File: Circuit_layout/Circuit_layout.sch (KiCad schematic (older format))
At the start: 34 parts, among them Q3 MMBF170, SW1 SW_PUSH, SW3 JS202011CQN, U17 MCP6004, U4 LM95071-Q1, U7 AT90CAN128-A, U9 TLP293, Y1 10MHz

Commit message: Completed errata changes
Committing before annotation, footprint assignment, and board relayout for backup purposes
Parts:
- Q3: symbol MMBF170 -> MMBF170-RESCUE-Circuit_layout
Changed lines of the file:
@@
 $EndComp
 $Comp
-L MMBF170 Q3
+L MMBF170-RESCUE-Circuit_layout Q3
 U 1 1 58D1260E
 P 5100 5350

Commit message: Associated footprints and generated new netlist
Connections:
- no-connect marks 20 -> 21
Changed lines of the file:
@@
 Wire Wire Line
 	9800 2000 9850 2000
+NoConn ~ 10450 3400
 $EndSCHEMATC

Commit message: Wider traces for DC/DC converter
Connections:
- no-connect marks 21 -> 20
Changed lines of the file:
@@
 Wire Wire Line
 	9800 2000 9850 2000
-NoConn ~ 10450 3400
 $EndSCHEMATC

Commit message: Generated gerber and drill files for board ordering
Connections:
- net CC_LED_CTRL renamed SPARE_LED_CTRL
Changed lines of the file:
@@
 F5 "Spare_Red" I L 11850 4150 60
 F6 "Spare_Blue" I L 11850 4300 60
-F7 "CC_LED_CTRL" I L 11850 3850 60
+F7 "SPARE_LED_CTRL" I L 11850 3850 60
 $EndSheet
 $Sheet
@@
 	8850 1250 8850 1150
 Text Label 11250 3850 0    60   ~ 0
-CC_LED_CTRL
+SPARE_LED_CTRL
 Wire Wire Line
 	11250 3850 11850 3850
@@
 	11250 4300 11850 4300
 Text Label 9850 2000 0    60   ~ 0
-CC_LED_CTRL
+SPARE_LED_CTRL
 Wire Wire Line
 	9800 2000 9850 2000

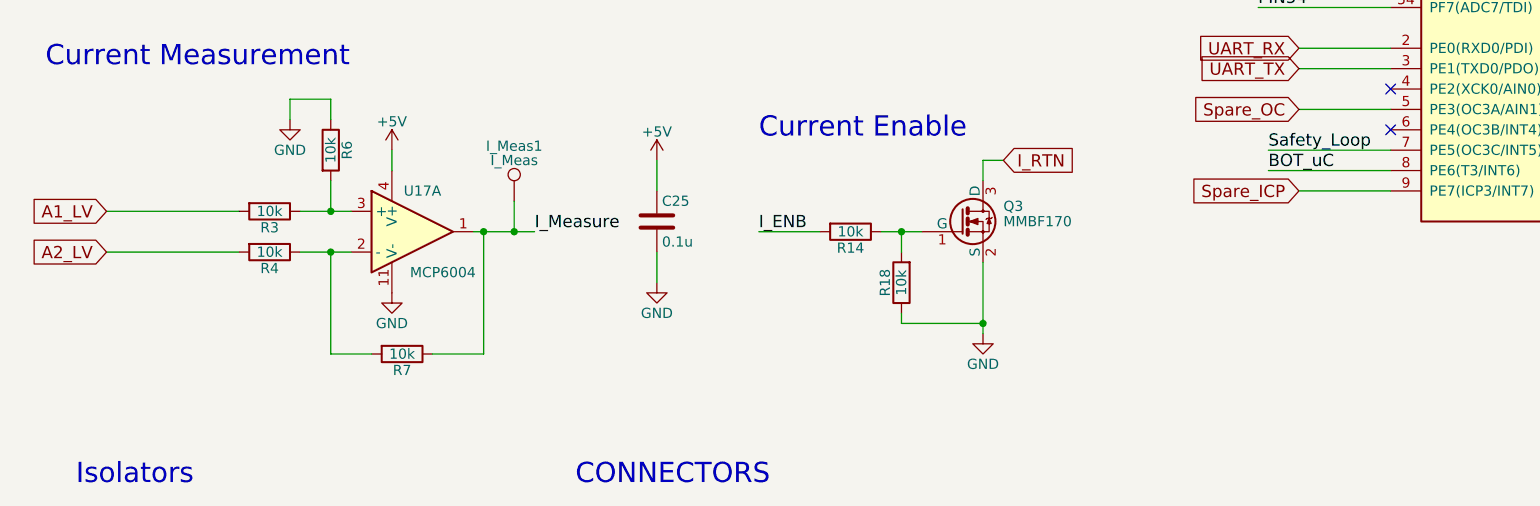
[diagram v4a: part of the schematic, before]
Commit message: Schematic update
Changed schematic to reflect board as assembeled
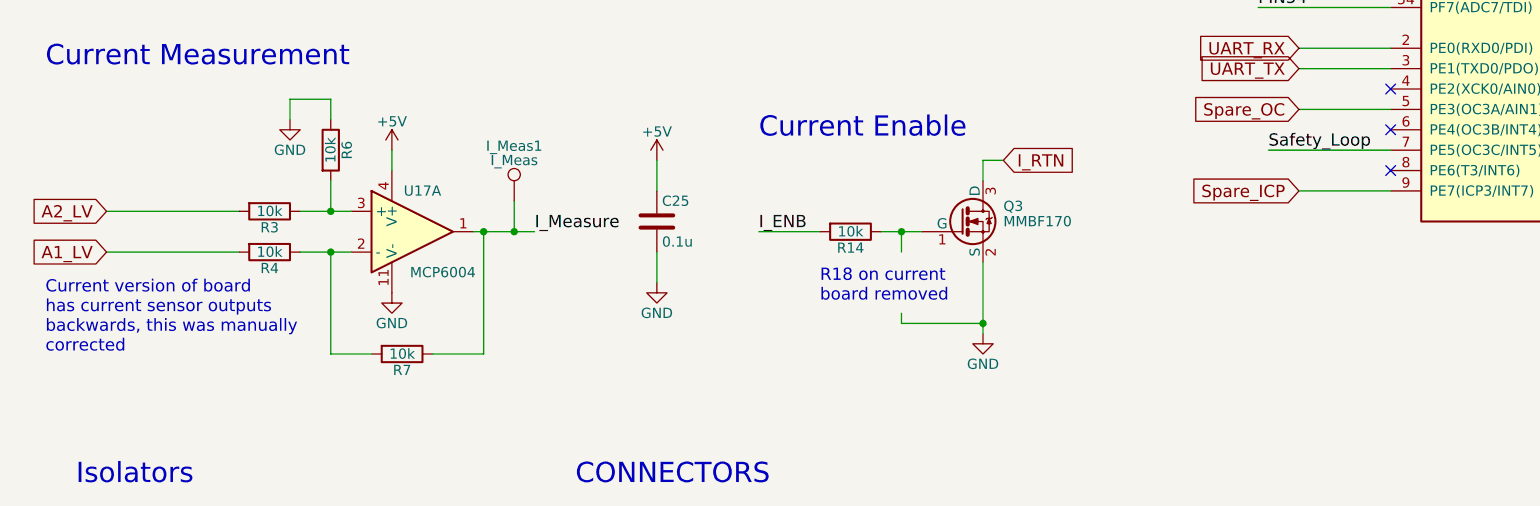
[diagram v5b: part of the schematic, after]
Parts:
- removed R18: 10k, Resistors_SMD:R_0805_HandSoldering, symbol R
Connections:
- net A1_LV: now also R4.2; no longer R3.2
- net A2_LV: now also R3.2; no longer R4.2
- net BOT_uC: no longer U7.8 (PE6(T3/INT6))
- no-connect marks 20 -> 21
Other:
- note added: "Current version of board\nhas current sensor outputs\nbackwards, this was manually\ncorrected"
- note added: "R18 on current\nboard removed"
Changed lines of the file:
@@
 LIBS:ftdi
 LIBS:gennum
-LIBS:graphic
 LIBS:hc11
 LIBS:intel
@@
 LIBS:Lattice
 LIBS:linear
-LIBS:logo
 LIBS:maxim
 LIBS:memory
@@
 Text Label 10450 3400 2    60   ~ 0
 Throttle_uC
+Text GLabel 900  5300 0    60   Input ~ 0
+A2_LV
 Text GLabel 900  5500 0    60   Input ~ 0
-A2_LV
-Text GLabel 900  5300 0    60   Input ~ 0
 A1_LV
 Text GLabel 9900 2300 2    60   Input ~ 0
@@
 Text Label 11100 6250 0    60   ~ 0
 BOT_uC
-Text Label 6600 5100 0    60   ~ 0
-BOT_uC
 $Comp
 L SW_PUSH SW1
@@
 $EndComp
 $Comp
-L R R18
-U 1 1 58D1580D
-P 4800 5650
-F 0 "R18" V 4880 5650 50  0000 C CNN
-F 1 "10k" V 4800 5650 50  0000 C CNN
-F 2 "Resistors_SMD:R_0805_HandSoldering" V 4730 5650 50  0001 C CNN
-F 3 "" H 4800 5650 50  0000 C CNN
-F 4 "P10.0KCCT-ND" V 4800 5650 60  0001 C CNN "DigiKey P/N"
-F 5 "http://www.digikey.com/product-detail/en/panasonic-electronic-components/ERJ-6ENF1002V/P10.0KCCT-ND/119248" V 4800 5650 60  0001 C CNN "URL"
-F 6 "ERJ-6ENF1002V" V 4800 5650 60  0001 C CNN "Man P/N"
-	1    4800 5650
-	-1   0    0    1
-$EndComp
-$Comp
 L GND #PWR019
 U 1 1 58D15ED8
@@
 Wire Wire Line
 	4700 5400 4900 5400
-Wire Wire Line
-	4800 5500 4800 5400
 Connection ~ 4800 5400
 Wire Wire Line
@@
 Text Notes 3800 2950 0    99   ~ 0
 Temp. Sensor
-Wire Wire Line
-	7200 5100 6600 5100
 NoConn ~ 9800 3600
 Wire Wire Line
@@
 Wire Wire Line
 	9800 2000 9850 2000
+NoConn ~ 7200 5100
+Text Notes 600  6000 0    60   ~ 0
+Current version of board\nhas current sensor outputs\nbackwards, this was manually\ncorrected
+Wire Wire Line
+	4800 5500 4800 5400
+Text Notes 4400 5750 0    60   ~ 0
+R18 on current\nboard removed
 $EndSCHEMATC
